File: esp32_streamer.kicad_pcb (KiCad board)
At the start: 6 copper layers, 44 parts, among them J1 USB4510-03-1-A, J2 SJ1-3533NS, J3 Conn_01x04_Male, U1 PCM5122PW, U2 ESP32-WROVER-EM213EH2864PH3Q0, U3 MCP1825S, U4 MCP1825S

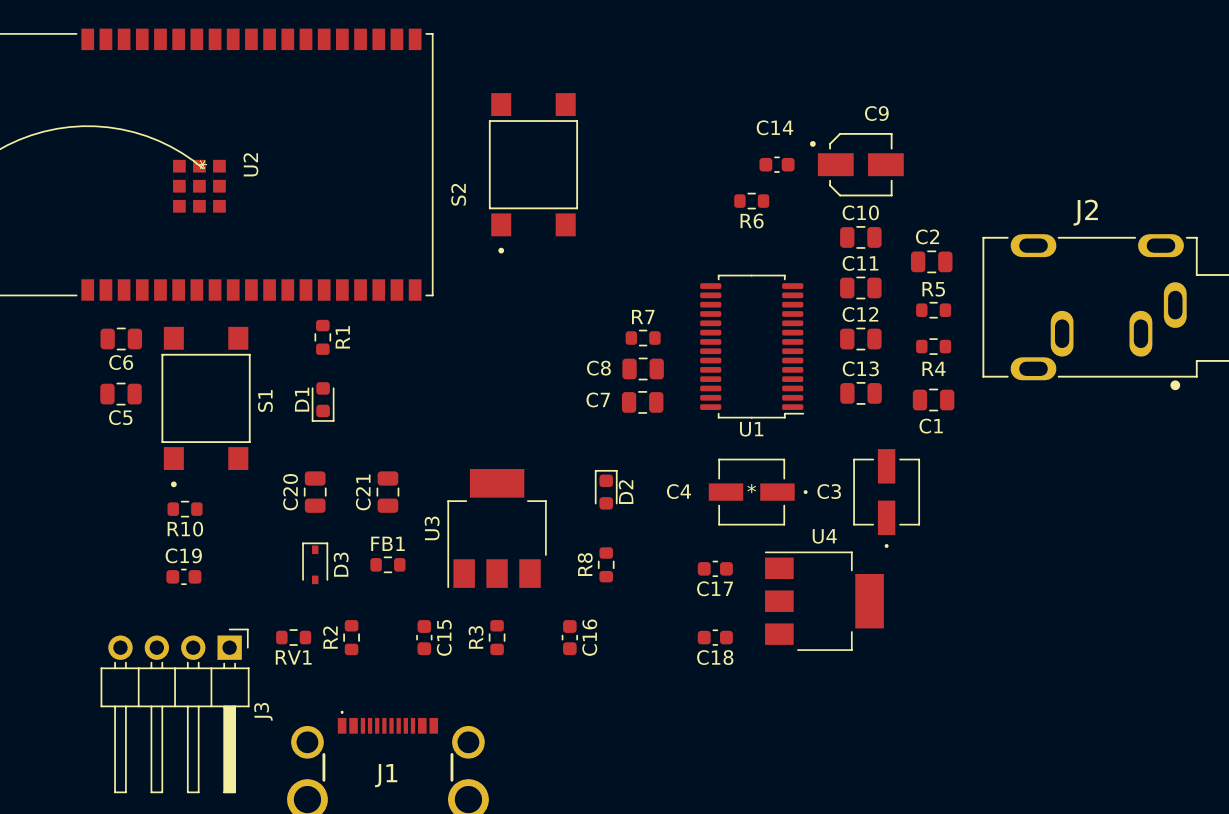
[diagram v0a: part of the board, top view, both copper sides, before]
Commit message: Added more traces and a ground plane
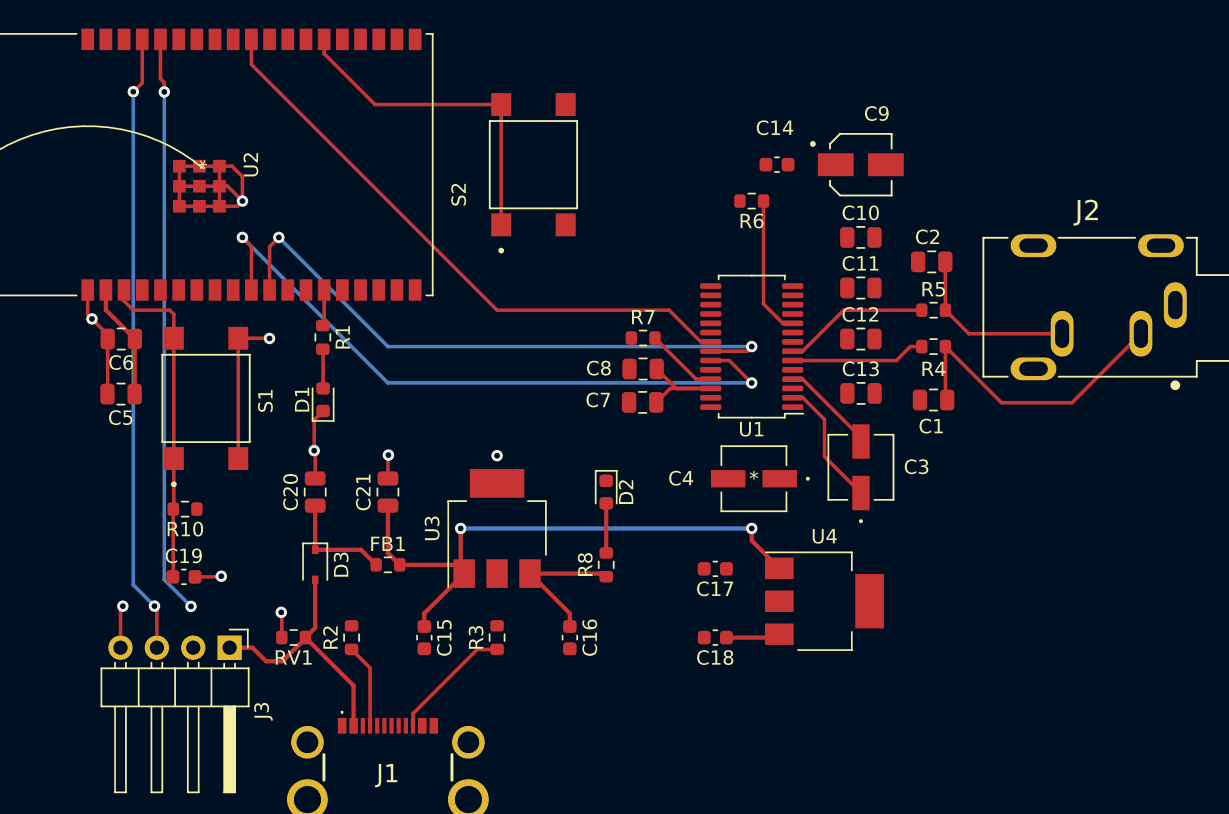
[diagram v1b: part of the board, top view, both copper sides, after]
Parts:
- moved C3 2.49 mm to (149.9, 120.2)
- moved C4 0.95 mm to (142.4, 121.0)
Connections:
- J3 pad 2: ESP32_Tx -> ESP32_Rx
- J3 pad 3: ESP32_Rx -> ESP32_Tx
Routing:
- net GND: track 0.00 -> 53.1 mm, vias 0 -> 9
- net PCM_LRCK: track 0.00 -> 47.2 mm, vias 0 -> 2
- net ESP32_Tx: track 0.00 -> 43.4 mm, vias 0 -> 2
- net PCM_DIN: track 0.00 -> 43.1 mm, vias 0 -> 2
- net PCM_BCK: track 0.00 -> 41.8 mm
- net ESP32_Rx: track 0.00 -> 40.5 mm, vias 0 -> 2
- net VBUS_FILT: track 0.00 -> 40.0 mm, vias 0 -> 2
- net GPIO0: track 0.00 -> 23.2 mm
- net RESET: track 0.00 -> 23.0 mm
- net Net-(C1-Pad2): track 0.00 -> 21.1 mm
- net +3V3: track 0.00 -> 18.4 mm
- net VBUS: track 0.00 -> 18.3 mm
- net Net-(C2-Pad1): track 0.00 -> 12.2 mm
- net Net-(R5-Pad1): track 0.00 -> 10.2 mm
- net Net-(R6-Pad1): track 0.00 -> 9.78 mm
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- added copper zone on In1.Cu, net GND

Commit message: Continued working on PCB - most traces laid out. Need to adhere to DRC rules though
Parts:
- moved C9 2.54 mm to (152.4, 99.1)
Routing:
- net GND: track 53.1 -> 175.4 mm, vias 9 -> 36
- net +3.3VA: track 4.31 -> 26.2 mm, vias 0 -> 7
- net Net-(C4-Pad1): track 0.00 -> 9.47 mm
- net +3V3: track 18.4 -> 27.2 mm, vias 0 -> 5
- net VBUS_FILT: track 40.0 -> 43.7 mm
- net PCM_DIN: track 43.1 -> 41.6 mm
- net PCM_LRCK: track 47.2 -> 45.7 mm
- added copper zone on In3.Cu, net +3.3VA
- added copper zone on In3.Cu, net +3V3
- added copper zone on In3.Cu, net GND
- added copper zone on In4.Cu, net GND

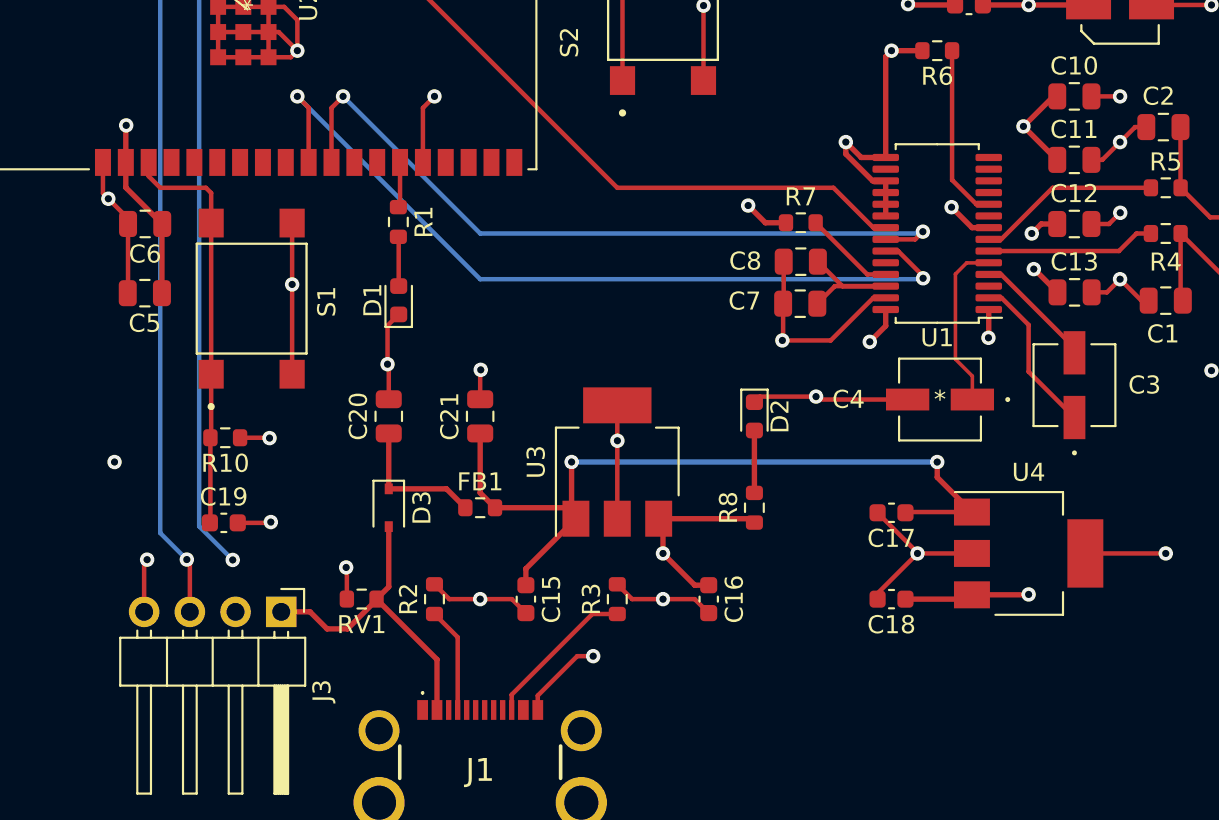
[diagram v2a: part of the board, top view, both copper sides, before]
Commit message: Fixes to footprints and added more traces. Need to fix all DRC errors & warnings next.
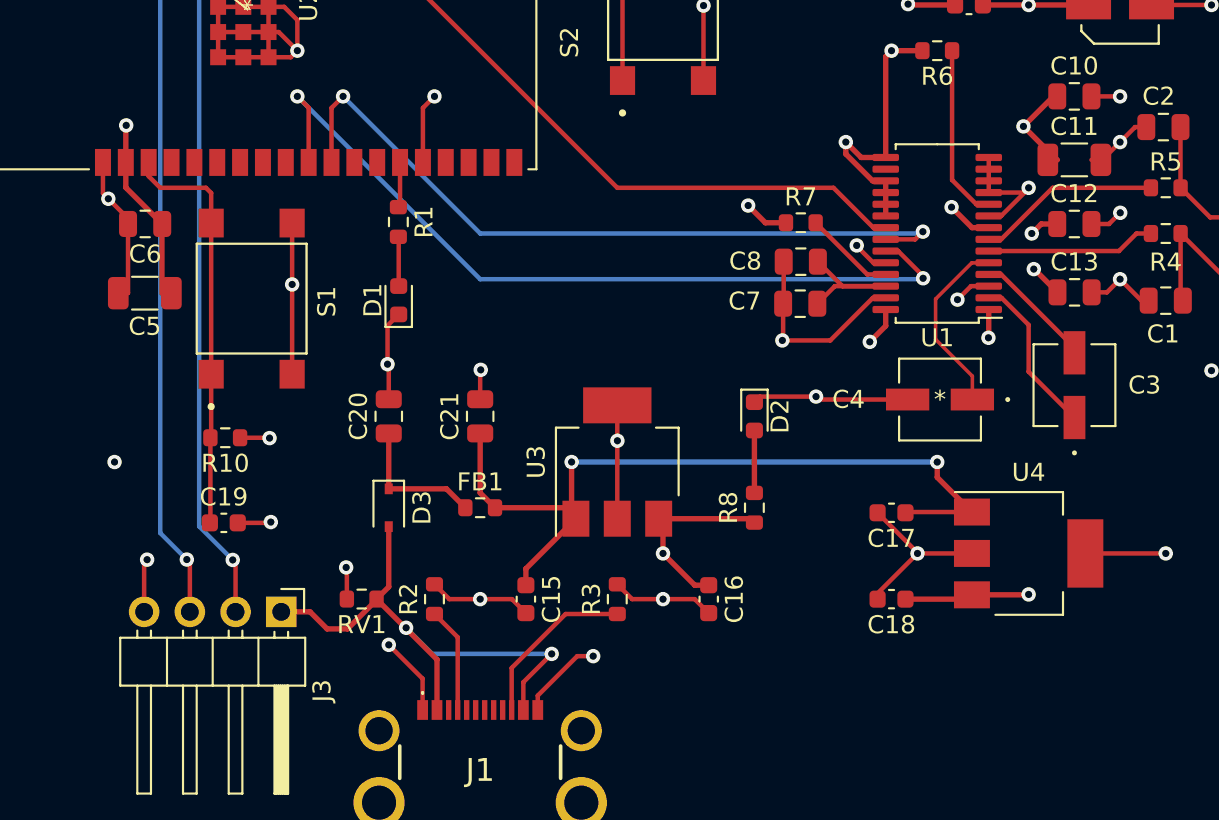
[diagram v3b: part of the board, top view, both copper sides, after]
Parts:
- C11, C5: footprint Capacitor_SMD:C_0805_2012Metric -> Capacitor_SMD:C_1206_3216Metric
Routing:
- net GND: track 175.4 -> 191.0 mm, vias 36 -> 40
- net VBUS: track 18.3 -> 30.7 mm, vias 0 -> 2
- net ESP32_Rx: track 40.5 -> 43.4 mm
- net Net-(J1-PadB5): track 8.58 -> 9.45 mm
- net Net-(C4-Pad1): track 9.47 -> 10.2 mm

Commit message: Sensible changes to grid and component placement for DAC (following TI datasheet)
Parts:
- C3, C4: value 2.2uF UUQ1H2R2MCL1GB -> 2.2uF
- J3: footprint Connector_PinHeader_2.54mm:PinHeader_1x04_P2.54mm_Horizontal -> Connector_PinHeader_2.54mm:PinHeader_1x04_P2.54mm_Vertical
- moved C9 37.1 mm to (148.5, 136.0)
- moved C10 33.1 mm to (143.0, 136.5), turned to 180 degrees
- moved C14 14.9 mm to (143.5, 114.0), turned to -90 degrees
- moved C13 13.2 mm to (147.6, 102.0)
- moved J2 11.1 mm to (162.4, 114.7), turned to 90 degrees
- moved R4 8.12 mm to (147.5, 108.5)
- moved R5 7.92 mm to (147.5, 106.5)
- moved C3 6.74 mm to (149.0, 113.5)
- moved C1 6.30 mm to (153.0, 109.5), turned to 90 degrees
- moved C12 5.14 mm to (145.5, 114.0), turned to -90 degrees
- moved U1 4.82 mm to (141.5, 107.0)
- moved C4 4.17 mm to (140.2, 117.4), turned to 90 degrees
- moved C18 4.09 mm to (143.0, 134.5)
- moved C11 3.67 mm to (148.0, 104.5)
- moved R7 3.44 mm to (136.0, 108.0)
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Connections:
- net Net-(C1-Pad2) renamed /JACKL
- net Net-(C2-Pad1) renamed /JACKR
- net Net-(C3-Pad1) renamed /CAPP
- net Net-(C3-Pad2) renamed /CAPM
- net Net-(C7-Pad1) renamed /LDO0
- net Net-(R4-Pad2) renamed /OUTL
- net Net-(R5-Pad1) renamed /OUTR
- net Net-(R6-Pad1) renamed /DEMP
- net Net-(R7-Pad2) renamed /XSMT
- C4 pad 1: Net-(C4-Pad1) -> GND
- C4 pad 2: GND -> /VNEG
- U1 pad 5: Net-(C4-Pad1) -> /VNEG
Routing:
- net GND: track 191.0 -> 99.1 mm, vias 40 -> 18
- net PCM_LRCK: track 45.7 -> 18.3 mm, vias 2 -> 1
- net PCM_DIN: track 41.6 -> 14.7 mm, vias 2 -> 1
- net +3.3VA: track 26.2 -> 0.00 mm, vias 7 -> 0
- net /JACKL: track 21.1 -> 0.00 mm
- net PCM_BCK: track 41.8 -> 26.0 mm
- net /JACKR: track 12.2 -> 0.00 mm
- net Net-(C4-Pad1): track 10.2 -> 0.00 mm
- net /OUTR: track 10.2 -> 0.00 mm
- net /DEMP: track 9.78 -> 0.00 mm
- net /OUTL: track 9.42 -> 0.00 mm
- net /CAPP: track 9.04 -> 0.00 mm
- net /LDO0: track 8.54 -> 0.00 mm
- net /CAPM: track 6.73 -> 0.00 mm
- net /XSMT: track 5.08 -> 0.00 mm
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
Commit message: Analog DAC components now laid out properly (hopefully).
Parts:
- added C22: 10uF, Capacitor_SMD:C_1206_3216Metric, F.Cu at (84.5, 114.0)
- added C23: 0.1uF, Capacitor_SMD:C_0805_2012Metric, F.Cu at (89.5, 113.8)
- moved U2 44.5 mm to (95.0, 55.5)
- moved C9 44.0 mm to (139.0, 93.0), turned to 180 degrees
- moved C10 40.1 mm to (146.0, 96.5), turned to 0 degrees
- moved C17 38.0 mm to (141.0, 89.0)
- moved C18 38.0 mm to (142.5, 96.5)
- moved U4 38.0 mm to (147.5, 91.5)
- moved C6 37.3 mm to (135.5, 112.0)
- moved C5 36.8 mm to (135.0, 114.5)
- moved S2 29.4 mm to (105.0, 79.5)
- moved R7 7.62 mm to (139.0, 101.0)
- moved D2 6.23 mm to (129.0, 116.5)
- moved C7 4.66 mm to (134.5, 108.5), turned to 90 degrees
- moved C8 1.84 mm to (136.5, 108.5), turned to 90 degrees
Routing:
- net GND: track 99.1 -> 48.7 mm, vias 18 -> 12
- net VBUS_FILT: track 40.0 -> 13.6 mm, vias 2 -> 0
- net PCM_BCK: track 26.0 -> 0.00 mm
- net GPIO0: track 23.2 -> 0.00 mm
- net +3V3: track 22.5 -> 12.4 mm, vias 3 -> 2
- net PCM_DIN: track 14.7 -> 10.8 mm, vias 1 -> 0
- net PCM_LRCK: track 18.3 -> 14.4 mm, vias 1 -> 0
- net ESP32_Tx: track 43.4 -> 39.5 mm, vias 2 -> 1
- net ESP32_Rx: track 43.4 -> 39.6 mm, vias 2 -> 1
- net RESET: track 23.0 -> 22.3 mm
- added copper zone on F.Cu, net GND

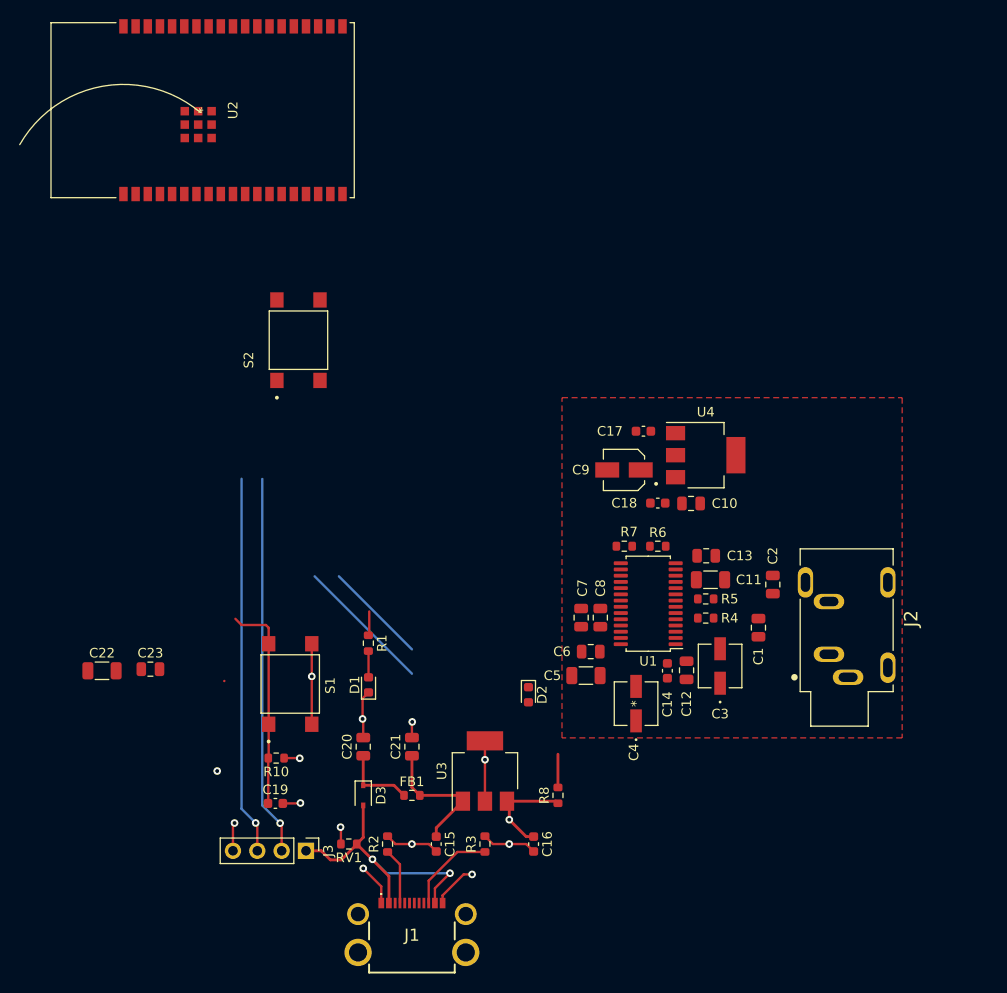
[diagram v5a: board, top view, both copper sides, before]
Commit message: Updated PCB layout - now it looks cleaner - completed layout. next step: traces
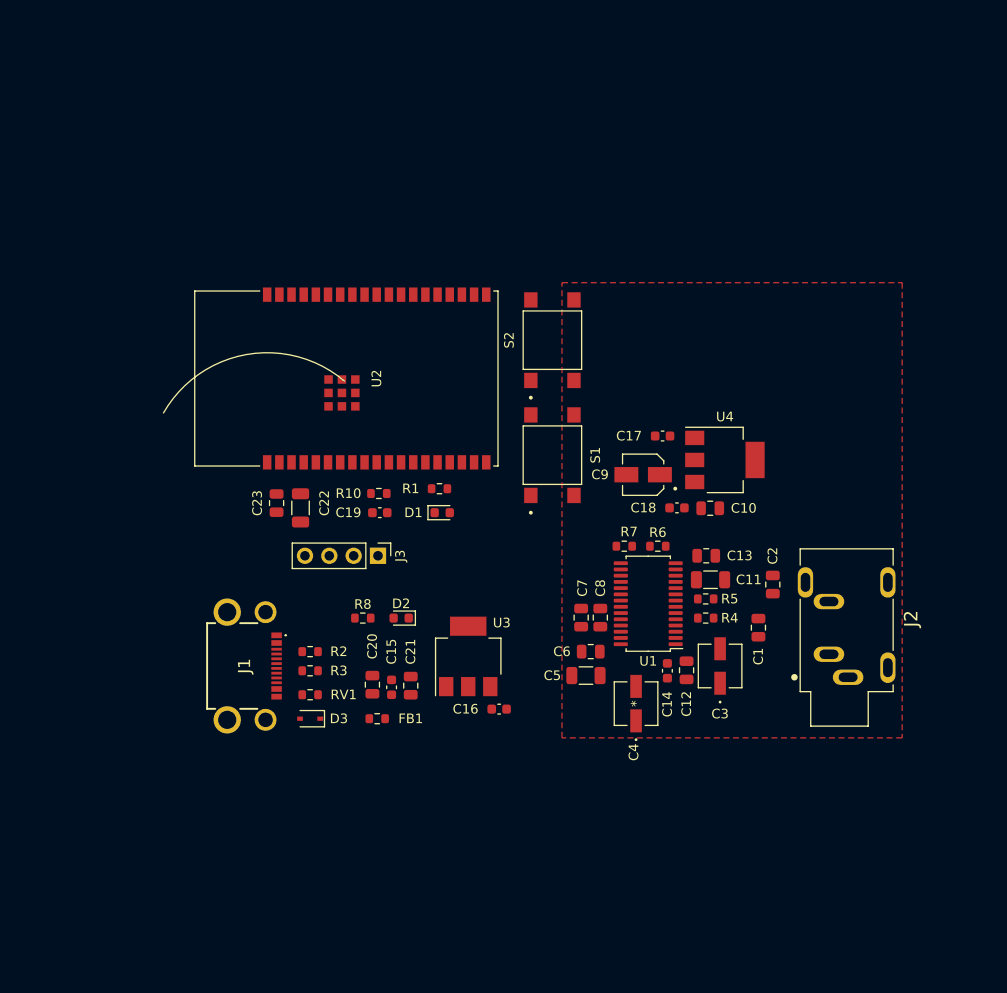
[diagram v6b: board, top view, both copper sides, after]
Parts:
- moved S1 36.3 mm to (131.5, 91.5)
- moved J1 34.0 mm to (98.7, 113.5), turned to -90 degrees
- moved C19 32.2 mm to (113.5, 97.5), turned to 180 degrees
- moved U2 31.8 mm to (110.0, 83.5)
- moved J3 31.7 mm to (113.3, 102.0)
- moved R10 29.6 mm to (113.4, 95.5), turned to 0 degrees
- moved R8 27.5 mm to (111.7, 108.5), turned to 0 degrees
- moved C22 26.8 mm to (105.2, 97.0), turned to -90 degrees
- moved S2 26.5 mm to (131.5, 79.5)
- moved R3 25.7 mm to (106.2, 114.0), turned to 0 degrees
- moved C23 21.8 mm to (102.7, 96.5), turned to -90 degrees
- moved R2 21.6 mm to (106.2, 112.0), turned to 0 degrees
- moved D1 19.5 mm to (120.0, 97.5), turned to 0 degrees
- moved R1 17.7 mm to (119.7, 95.0), turned to 0 degrees
- moved C15 17.0 mm to (114.7, 115.7), turned to 90 degrees
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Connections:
- net Net-(D1-Pad2) renamed /D1_PWR
- net Net-(D2-Pad2) renamed /D2_PWR
- net Net-(J1-PadA5) renamed /CC1
- net Net-(J1-PadB5) renamed /CC2
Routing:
- net GND: track 48.7 -> 0.06 mm, vias 12 -> 0
- net ESP32_Rx: track 39.6 -> 0.00 mm, vias 1 -> 0
- net ESP32_Tx: track 39.5 -> 0.00 mm, vias 1 -> 0
- net VBUS: track 30.7 -> 0.00 mm, vias 2 -> 0
- net RESET: track 22.3 -> 0.00 mm
- net PCM_LRCK: track 14.4 -> 0.00 mm
- net VBUS_FILT: track 13.6 -> 0.00 mm
- net +3V3: track 12.4 -> 0.00 mm, vias 2 -> 0
- net PCM_DIN: track 10.8 -> 0.00 mm
- net /CC2: track 9.45 -> 0.00 mm
- net /VBUS_RP: track 7.77 -> 0.00 mm
- net /CC1: track 5.87 -> 0.00 mm
- net /D2_PWR: track 3.47 -> 0.00 mm
- net /D1_PWR: track 2.74 -> 0.00 mm
- net /GPIO12: track 2.52 -> 0.00 mm
- removed copper zone on In3.Cu, net +3.3VA
- removed copper zone on In3.Cu, net +3V3
- removed copper zone on In1.Cu, net GND
- removed copper zone on In3.Cu, net GND
- removed copper zone on In4.Cu, net GND
